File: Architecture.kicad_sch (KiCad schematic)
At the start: 0 parts

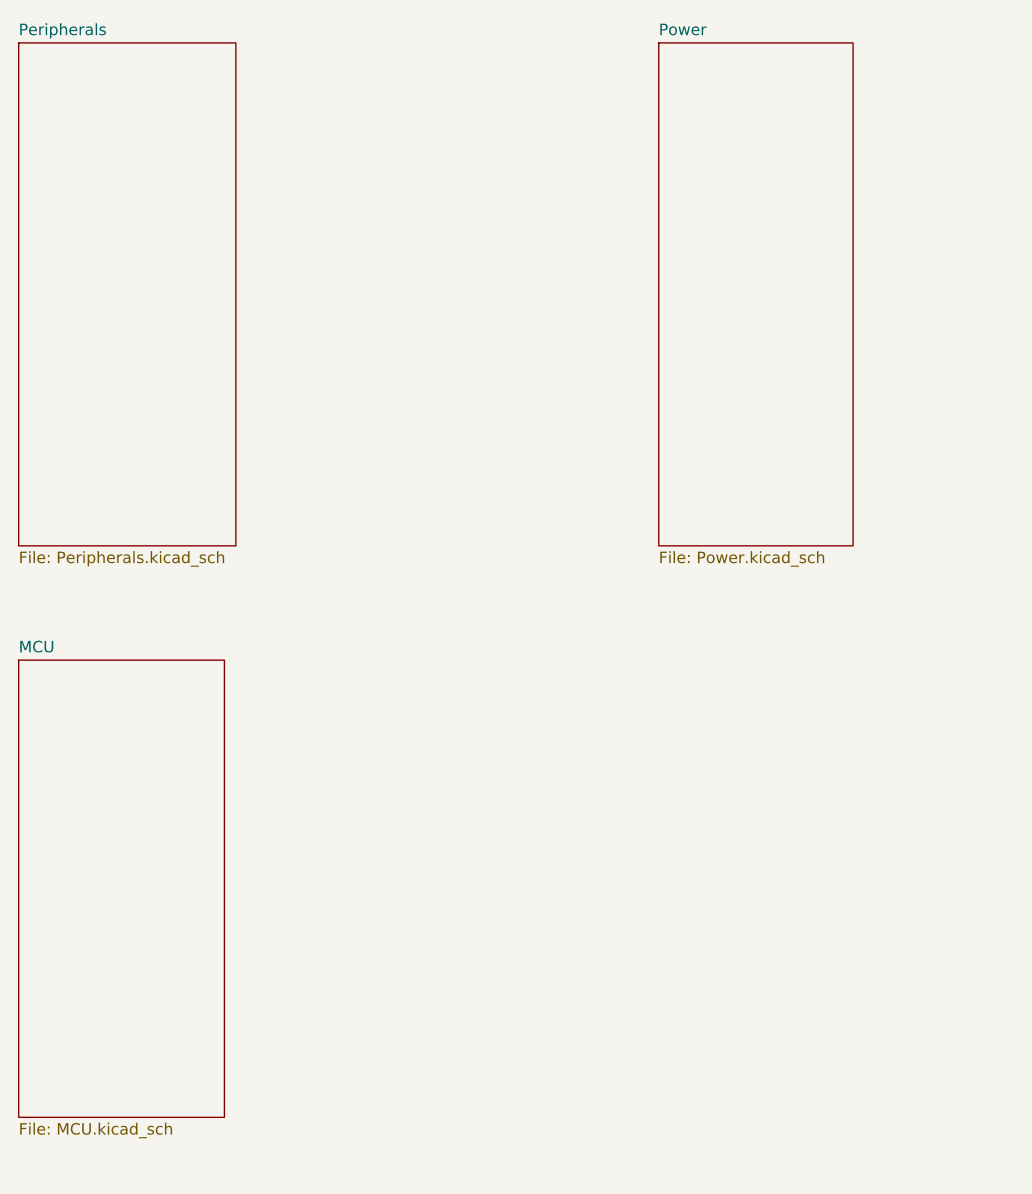
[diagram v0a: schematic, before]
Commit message: Fixed Hierarchical Labels
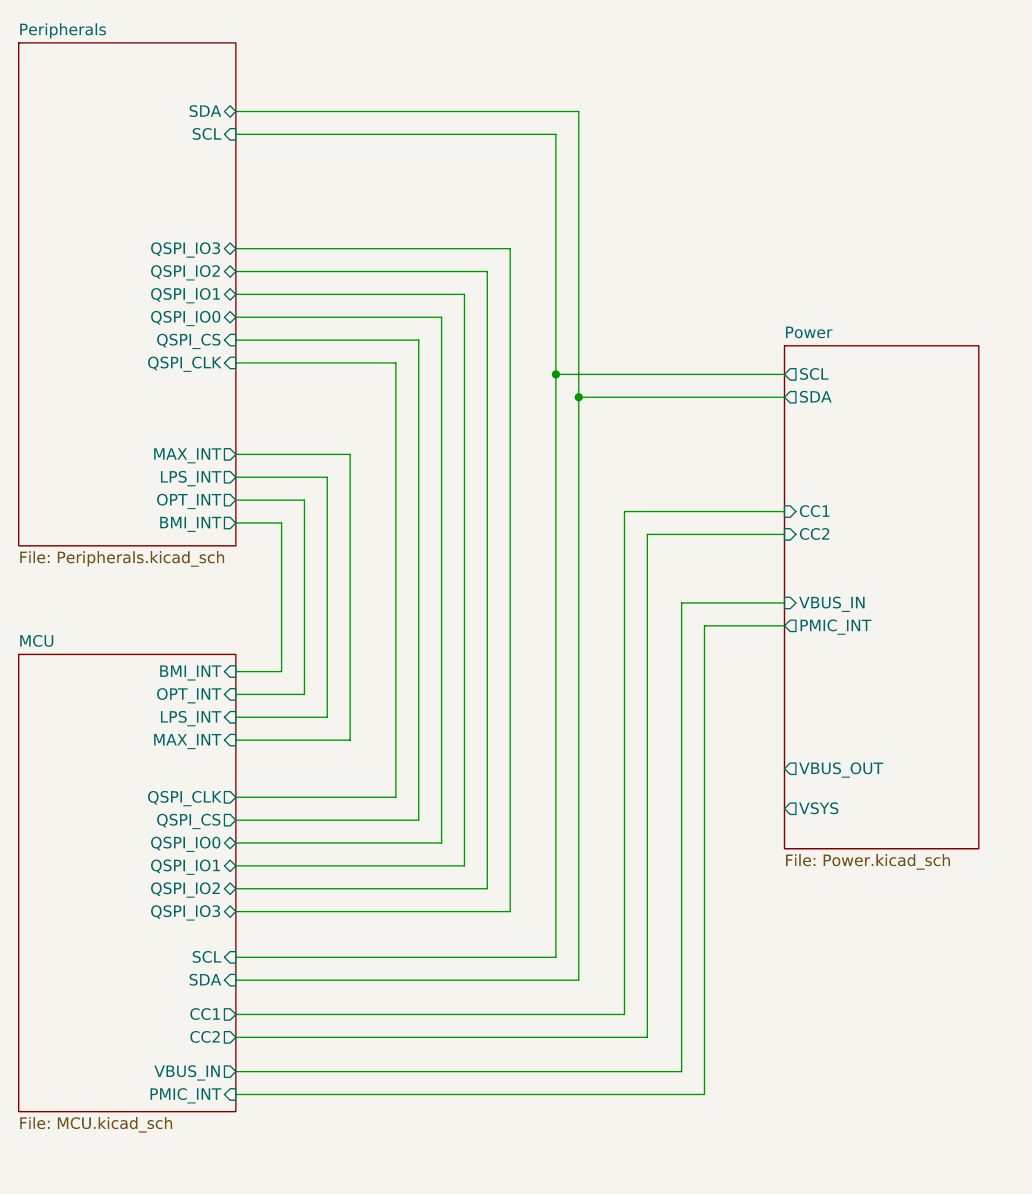
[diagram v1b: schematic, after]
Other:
- sheet MCU ports: added BMI_INT, CC1, CC2, LPS_INT, MAX_INT, OPT_INT, PMIC_INT, QSPI_CLK, QSPI_CS, QSPI_IO0, QSPI_IO1, QSPI_IO2, QSPI_IO3, SCL, SDA, VBUS_IN; removed none
- sheet Peripherals ports: added BMI_INT, LPS_INT, MAX_INT, OPT_INT, QSPI_CLK, QSPI_CS, QSPI_IO0, QSPI_IO1, QSPI_IO2, QSPI_IO3, SCL, SDA; removed none
- sheet Power ports: added CC1, CC2, PMIC_INT, SCL, SDA, VBUS_IN, VBUS_OUT, VSYS; removed none

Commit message: Added Vibration Motor & Prog Pinout
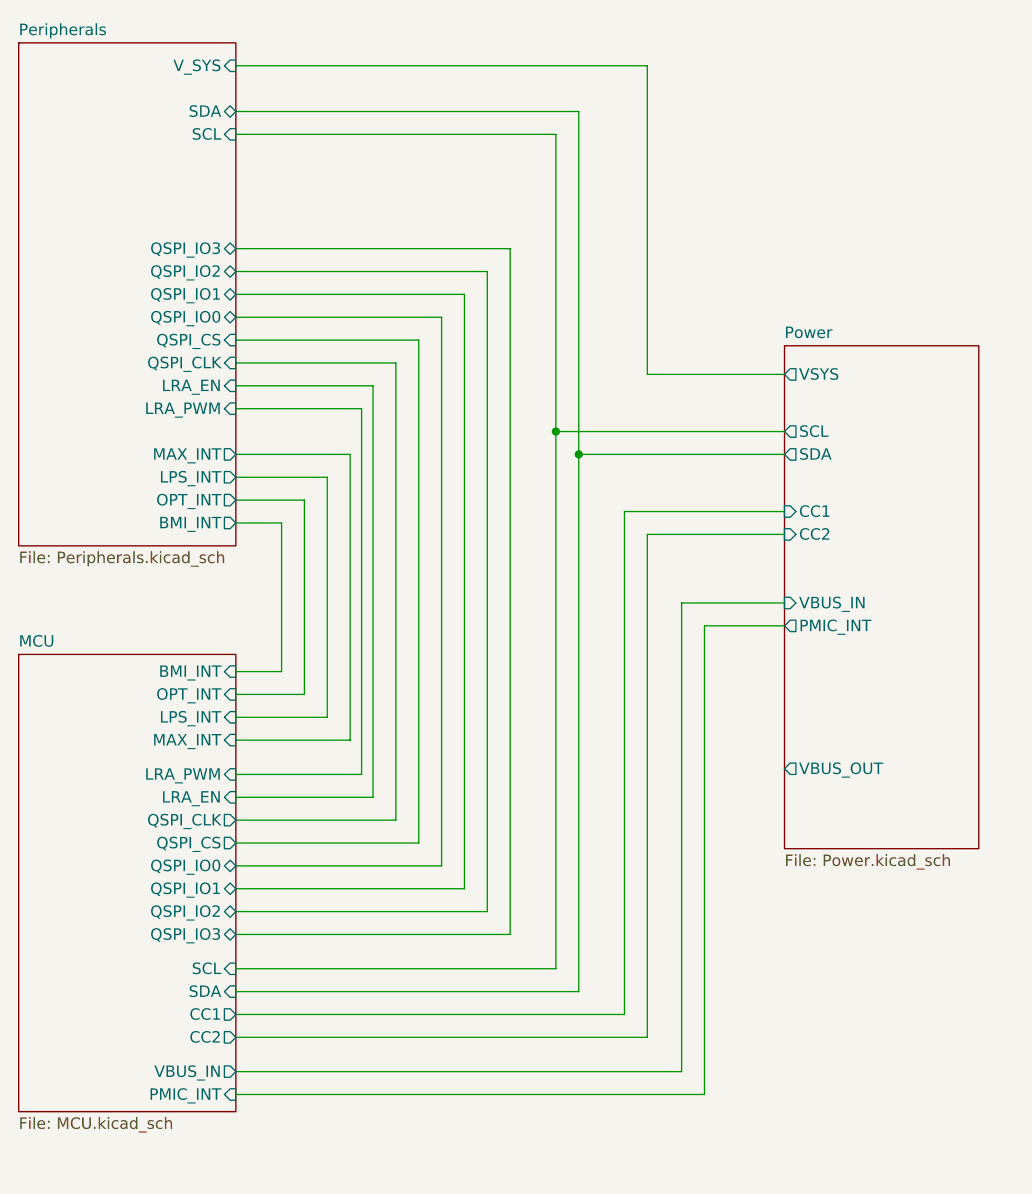
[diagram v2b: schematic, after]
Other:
- sheet MCU ports: added LRA_EN, LRA_PWM; removed none
- sheet Peripherals ports: added LRA_EN, LRA_PWM, V_SYS; removed none

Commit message: Added clock and updated schem
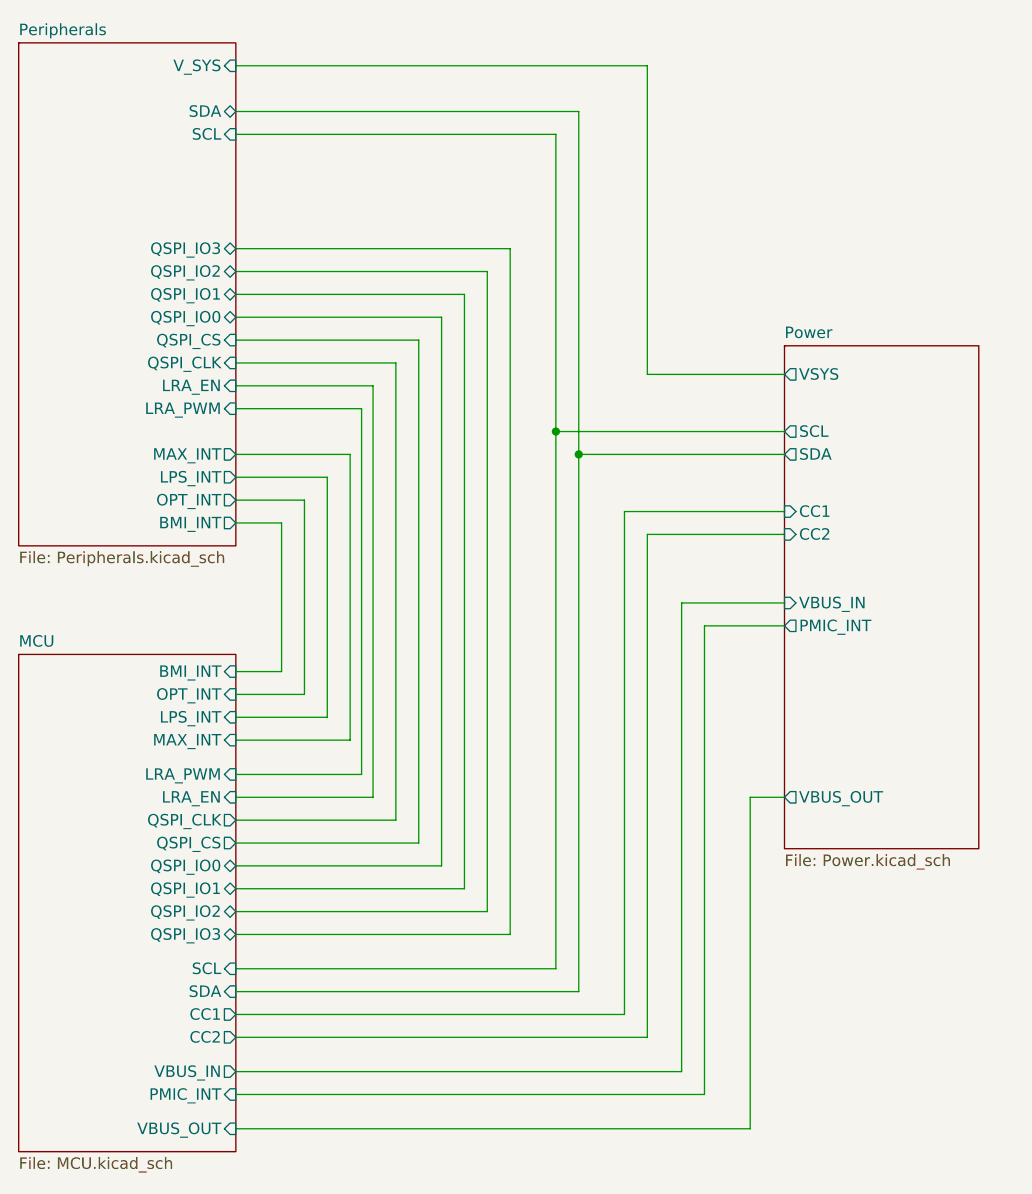
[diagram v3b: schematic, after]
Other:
- sheet MCU ports: added VBUS_OUT; removed none
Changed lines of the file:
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@@
+	(wire
+		(pts
+			(xy 118.11 163.83) (xy 118.11 127)
+		)
+		(stroke
+			(width 0)
+			(type default)
+		)
+	)
 	(wire
 		(pts
@@
 	(wire
 		(pts
+			(xy 118.11 127) (xy 121.92 127)
+		)
+		(stroke
+			(width 0)
+			(type default)
+		)
+	)
+	(wire
+		(pts
 			(xy 60.96 148.59) (xy 99.06 148.59)
 		)
@@
 		(pts
 			(xy 76.2 127) (xy 76.2 81.28)
+		)
+		(stroke
+			(width 0)
+			(type default)
+		)
+	)
+	(wire
+		(pts
+			(xy 60.96 163.83) (xy 118.11 163.83)
 		)
 		(stroke
@@
 	(sheet
 		(at 36.83 111.125)
-		(size 24.13 50.8)
+		(size 24.13 55.245)
 		(exclude_from_sim no)
 		(in_bom yes)
@@
 		)
 		(property "Sheetfile" "MCU.kicad_sch"
-			(at 36.83 162.5096 0)
+			(at 36.83 166.9546 0)
 			(effects
 				(font
@@
 		(pin "LRA_PWM" input
 			(at 60.96 124.46 0)
+			(effects
+				(font
+					(size 1.27 1.27)
+				)
+				(justify right)
+			)
+		)
+		(pin "VBUS_OUT" input
+			(at 60.96 163.83 0)
 			(effects
 				(font
@@
 		)
 		(pin "VBUS_OUT" output
-			(at 121.92 123.825 180)
-			(effects
-				(font
+			(at 121.92 127 180)
+			(effects
+				(font

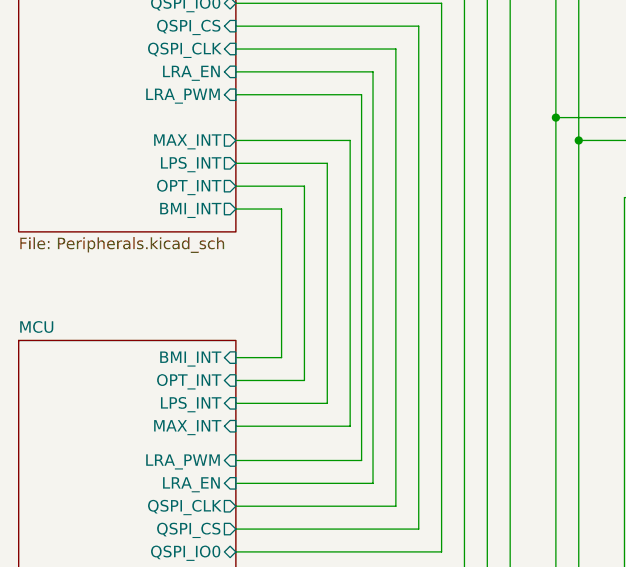
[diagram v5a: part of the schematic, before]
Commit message: Removed amb light, extended board for usbc and buttons
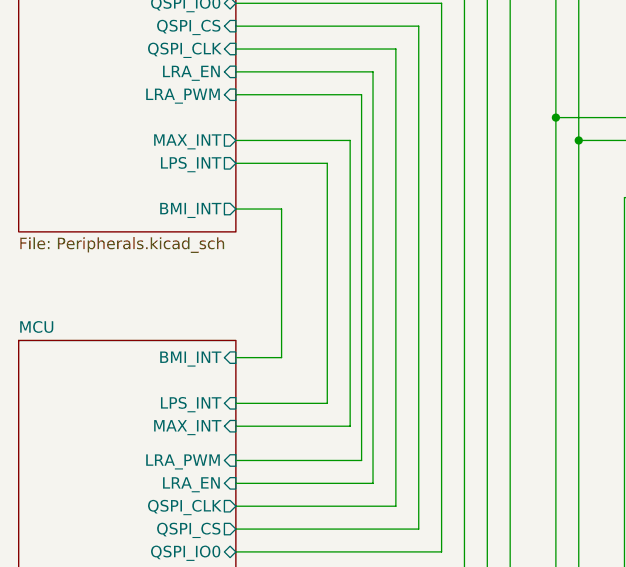
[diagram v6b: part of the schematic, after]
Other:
- sheet MCU ports: added none; removed OPT_INT
- sheet Peripherals ports: added none; removed OPT_INT
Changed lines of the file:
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@@
-	(wire
-		(pts
-			(xy 68.58 93.98) (xy 60.96 93.98)
-		)
-		(stroke
-			(width 0)
-			(type default)
-		)
-	)
 	(wire
 		(pts
@@
 	(wire
 		(pts
-			(xy 60.96 115.57) (xy 68.58 115.57)
-		)
-		(stroke
-			(width 0)
-			(type default)
-		)
-	)
-	(wire
-		(pts
 			(xy 60.96 124.46) (xy 74.93 124.46)
 		)
@@
 		(pts
 			(xy 99.06 88.9) (xy 121.92 88.9)
-		)
-		(stroke
-			(width 0)
-			(type default)
-		)
-	)
-	(wire
-		(pts
-			(xy 68.58 115.57) (xy 68.58 93.98)
 		)
 		(stroke
@@
 			)
 		)
-		(pin "OPT_INT" output
-			(at 60.96 93.98 0)
-			(effects
-				(font
-					(size 1.27 1.27)
-				)
-				(justify right)
-			)
-		)
 		(pin "QSPI_CLK" input
 			(at 60.96 78.74 0)
@@
 			(effects
 				(font
-					(size 1.27 1.27)
-				)
-				(justify right)
-			)
-		)
-		(pin "OPT_INT" input
-			(at 60.96 115.57 0)
-			(effects
-				(font
